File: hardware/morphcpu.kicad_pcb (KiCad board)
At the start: 4 copper layers, 70 x 70 mm, 84 parts, among them J1 TYPE-C-31-M-12, SW1 TS-1187A-B-A-B, U1 ICE40UP5K-SG48I, U2 FT231XS-R, U3 W25Q32JVSSIQ, U4 ME6211C33M5G-N, U5 ME6211C12M5G-N, U6 USBLC6-2SC6, X1 1532H4-16000JWPDTSNL

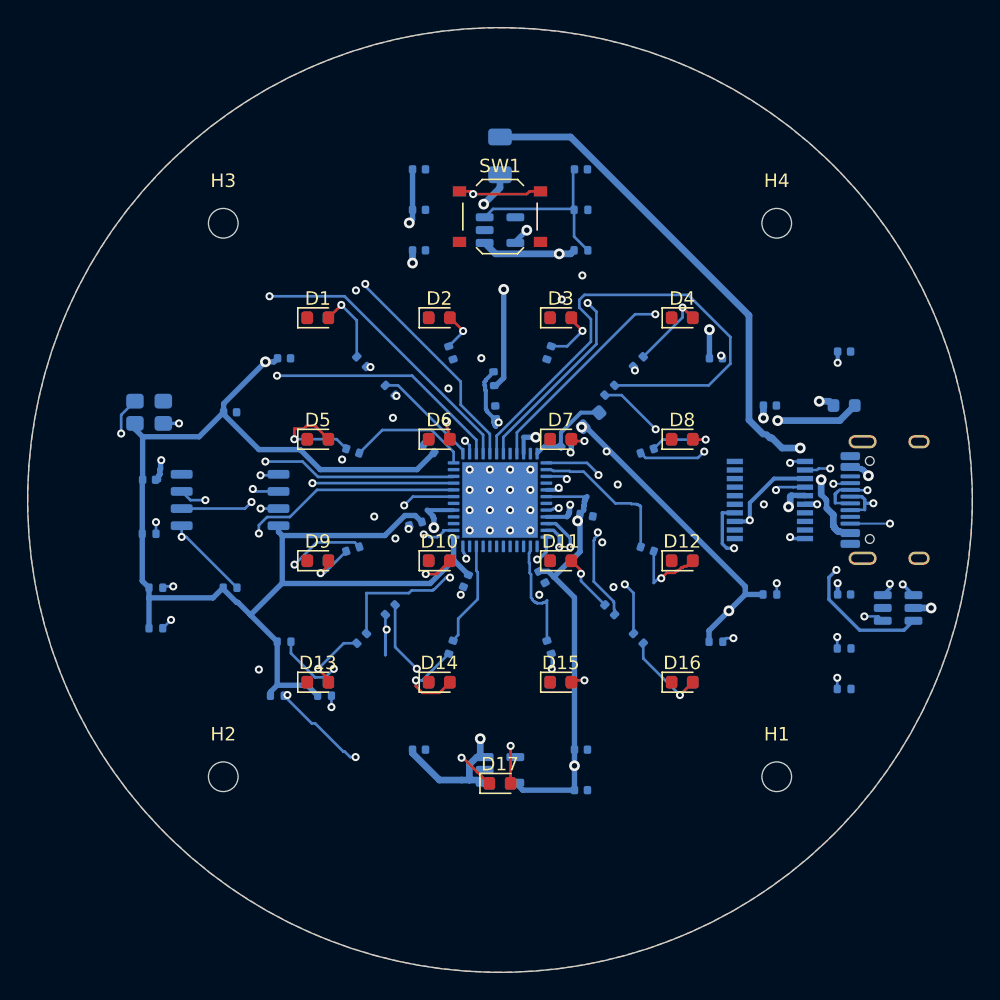
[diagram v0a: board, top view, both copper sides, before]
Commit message: silkscreen / board had none
only graphic on it was the edge cuts circle. front gets the name as eight
separate texts round r=29.7 rotated to the tangent cuz kicad has no curved
text, a frame circle at 32.9, IN and OUT arrows on the side lobes and eight
boxed direction arrows for what a cell can pick

back gets the name up top, url and iCE40UP5K SG48 and rev straight in the
bottom band. no frame circle that side, it crossed J1's outline at 182,95.3
and 182,104.7

mirrored arc text needs the run reversed and not just the glyphs, first pass
read UPCHPROM. first back pass also put the url's c and t into the H3 and H4
NPTH pads, 4 silk warnings, both gone now

DRC 0 violations, 2 unconnected, same two leds as before. no copper moved
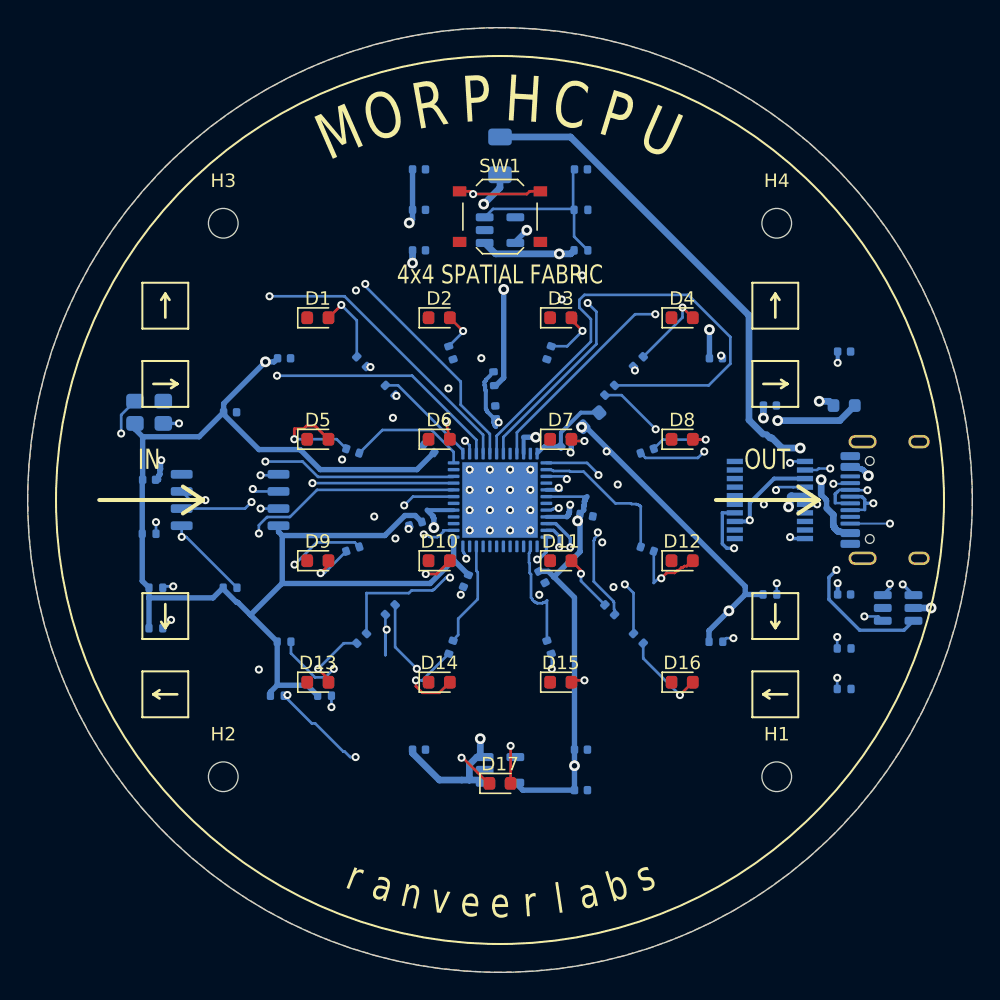
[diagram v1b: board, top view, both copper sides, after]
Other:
- board text added: "4x4 SPATIAL FABRIC"
- board text added: "C"
- board text added: "H"
- board text added: "IN"
- board text added: "M"
- board text added: "O"
- board text added: "OUT"
- board text added: "P"
- board text added: "R"
- board text added: "U"
- board text added: "a"
- board text added: "b"
- board text added: "e"
- board text added: "github.com/ranveerlabs/morphcpu"
- board text added: "iCE40UP5K SG48"
- board text added: "l"
- board text added: "n"
- board text added: "r"
- board text added: "rev A 2026"
- board text added: "s"
- board text added: "v"

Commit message: rev A off the back
sch_revision is empty and theres no earlier spin, so the board was carrying a
revision letter that nothing in the project backs. url and iCE40UP5K SG48 stay

DRC 0 violations, 2 unconnected, unchanged
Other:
- board text removed: "rev A 2026"
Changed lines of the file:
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@@
-		)
-	)
-	(gr_text "rev A  2026"
-		(at 150 131.199999 0)
-		(layer "B.SilkS")
-		(effects
-			(font
-				(size 1.3 1.014)
-				(thickness 0.22)
-			)
-			(justify mirror)
 		)
 	)

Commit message: decoupling caps onto their pins / stitching vias
the 6.5mm ring in gen_pcb.py placed the seven 100n by refdes order, so which
cap landed near which supply pin was arbitrary. measured as real copper path
not straight line, pin 22 was being decoupled by C12 under the FT231X at
49.31mm and pin 33 at 49.73mm. C4 and C5 were dead end spurs off the west
+3V3 trunk doing nothing for U1 at all

C3 -> pin 1 3.23 -> 1.16mm, C5 -> pin 22 49.31 -> 1.98mm, C21 -> pin 24
1.99 -> 1.13mm. deleted C5's 14.8mm dead end out to 132.14,96.27 and the
3.8mm stub it left dangling

every cap ground pad now has a via within 0.50mm with a 0.4mm tie so it
bypasses the thermal relief. C20 was 3.69mm off the nearest one and C5 3.03mm,
that was most of their loop

27 stitching vias at B.Cu island crossings under In2 traces. In2 references
B.Cu at 0.21mm and that pour is in 7 pieces, so a trace crossing a split had
the return current detouring to the nearest via. CRESET_B at 132.13,107.32 was
16.27mm and FLASH_HOLD at 126.84,107.68 was 15.11mm, both under 2mm now. two
crossings had no room, VBUS at 145.02,88.69 and +1V2 at 151.55,97.19

0 violations, 2 unrouted, same two LED nets as before
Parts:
- moved C5 8.47 mm to (153.1, 94.7), turned to 0 degrees
- moved C3 3.22 mm to (145.3, 103.7), turned to 180 degrees
- moved C21 0.83 mm to (154.1, 95.8), turned to 0 degrees
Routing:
- net +3V3: track 208.3 -> 192.3 mm
- net GND: track 4.70 -> 9.15 mm, vias 30 -> 64
- net VPP_2V5: track 6.44 -> 5.93 mm

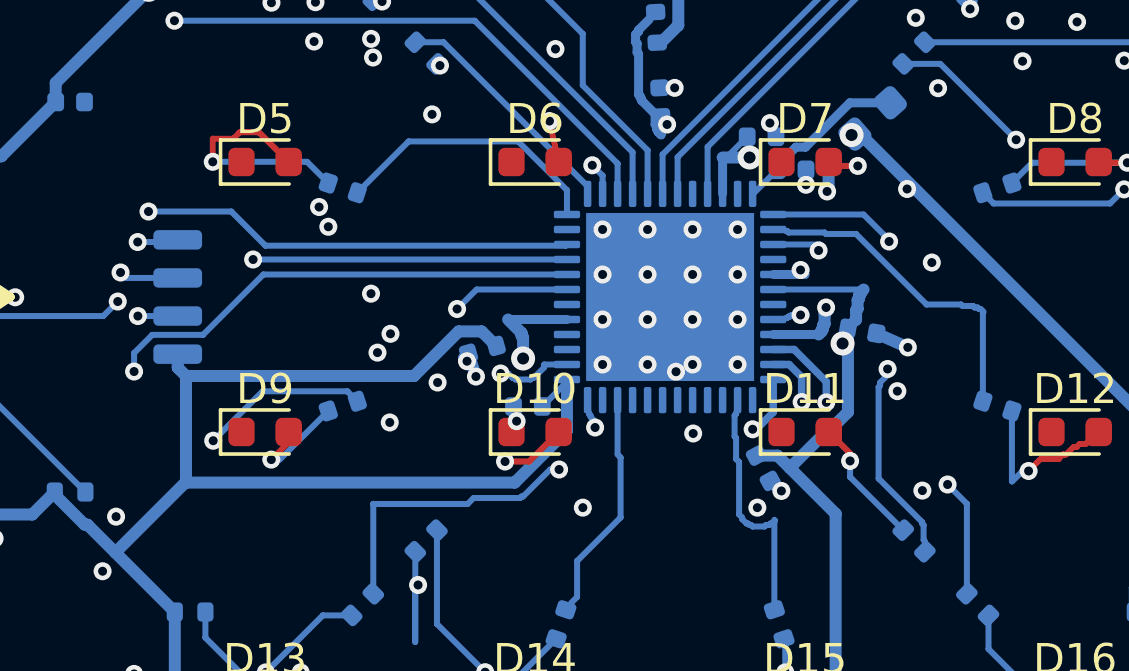
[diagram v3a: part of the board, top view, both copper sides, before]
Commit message: east face reshuffle / C4 across to pin 33
pins 29 30 and 33 all escape east and the lane at x 154-157 was full, so none
of them could have a cap next to them. moved the caps out to x=155.5375 instead
of hard against the pad row and most of the lane traffic stopped mattering

C1 -> pin 30, 156.401,101.129 -> 155.5375,99.90, path 3.24 -> 1.47mm
C4 -> pin 33, 143.743,101.760 -> 155.5375,101.25, path 49.73 -> 1.62mm
C2 -> pin 5, 153.109,105.708 -> 144.9625,100.75, path 13.77 -> 1.12mm

C4 crossing the board took its 11.2mm west dead end spur with it, and that spur
was what walled C2's ground pad onto a 1.58mm2 scrap of B.Cu pour with no room
for a via anywhere inside it. with the spur gone C2 has 251 placements with a
ground via, it had 0

LED11 LED15 and UART_TX_O did not need touching. checked each against the new
pads, LED11 clears C20 by 0.59mm, LED15's via at 154.350,100.600 sits 0.279mm
off C1 and 0.246mm off C4, UART clears C4 by 0.464mm. left as routed

three feeds rebuilt. +1V2 from the U5 trunk tip 7.11mm on In2 necked to 0.30
through the 0.72mm gap between LED15's via and C1's ground pad, the In1 tie to
pin 5 re-landed 5.24mm, +3V3 out of C4 6.22mm on In1 to the B.Cu diagonal

pin 29 still has no cap. with LED3 where it is C20 has 582 positions where it
fits with a clear courtyard and 0 with a routable stub. strip LED3 and C20
places at 1.76mm, but LED3's only via pocket is x 154.6-155.3 y 98.2-98.8 which
is exactly under C20's pad, and it cant go up either, a via between LED10 at
97.25 and LED3 at 98.25 needs 0.6mm clear of both which leaves nothing

one more stitching via, VBUS at 145.02,97.91, 4.97 -> 0.91mm. that crossing is
new, pulling C4's spur reshaped the pour there

six of seven supply pins under 2mm now. 0 violations, 2 unrouted
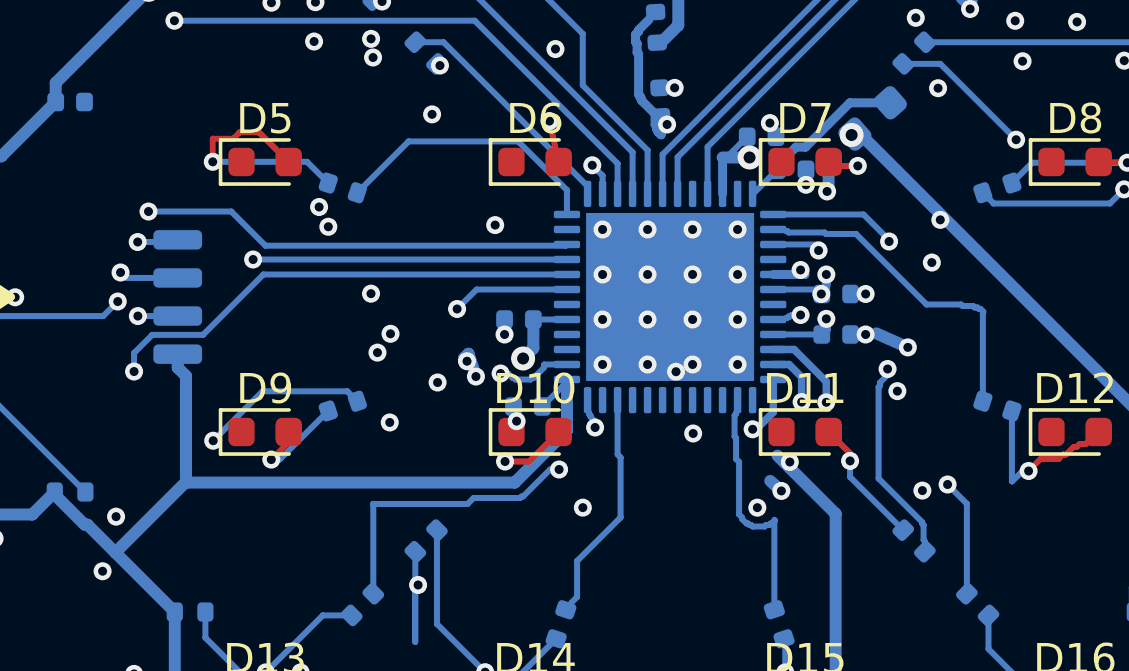
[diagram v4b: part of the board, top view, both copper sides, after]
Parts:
- moved C4 11.8 mm to (155.5, 101.2), turned to 0 degrees
- moved C2 9.54 mm to (145.0, 100.8), turned to 180 degrees
- moved C1 1.50 mm to (155.5, 99.9), turned to 0 degrees
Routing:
- net +3V3: track 192.3 -> 181.4 mm
- net +1V2: track 91.3 -> 94.0 mm, vias 4 -> 6
- net GND: track 9.15 -> 10.6 mm, vias 64 -> 68

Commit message: 2 LEDSS!!!1!!!1!
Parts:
- C1, C10, C11, C12, C13, C14, C15, C16, C17, C18, C19, C2, C20, C21, C3, C4, C5, C6, C7, C8, C9: footprint C_0402_1005Metric -> Capacitor_SMD:C_0402_1005Metric
- D1, D10, D11, D12, D13, D14, D15, D16, D17, D2, D3, D4, D5, D6, D7, D8, D9: footprint LED_0603_1608Metric -> LED_SMD:LED_0603_1608Metric
- F1: footprint Fuse_1206_3216Metric -> Fuse:Fuse_1206_3216Metric
- FB1, FB2: footprint L_0603_1608Metric -> Inductor_SMD:L_0603_1608Metric
- H1, H2, H3, H4: footprint MountingHole_2.2mm_M2 -> MountingHole:MountingHole_2.2mm_M2
- J1: footprint USB_C_Receptacle_HRO_TYPE-C-31-M-12 -> Connector_USB:USB_C_Receptacle_HRO_TYPE-C-31-M-12
- R1, R10, R11, R12, R13, R14, R15, R16, R17, R18, R19, R2, R20, R21, R22, R23, R24, R25, R27, R28, R29, R3, R30, R4, R5, R6, R7, R8, R9: footprint R_0402_1005Metric -> Resistor_SMD:R_0402_1005Metric
- R26: value 10k -> 1M; footprint R_0402_1005Metric -> Resistor_SMD:R_0402_1005Metric
- SW1: footprint SW_Push_1P1T_XKB_TS-1187A -> Button_Switch_SMD:SW_Push_1P1T_XKB_TS-1187A
- U1: footprint QFN-48-1EP_7x7mm_P0.5mm_EP5.6x5.6mm -> Package_DFN_QFN:QFN-48-1EP_7x7mm_P0.5mm_EP5.6x5.6mm
- U2: footprint SSOP-20_3.9x8.7mm_P0.635mm -> Package_SO:SSOP-20_3.9x8.7mm_P0.635mm
- U3: footprint SOIC-8_5.3x5.3mm_P1.27mm -> Package_SO:SOIC-8_5.3x5.3mm_P1.27mm
- U4: value ME6211C33M5G-N -> AP2112K-3.3TRG1; footprint SOT-23-5 -> Package_TO_SOT_SMD:SOT-23-5
- U5: footprint SOT-23-5 -> Package_TO_SOT_SMD:SOT-23-5
- U6: footprint SOT-23-6 -> Package_TO_SOT_SMD:SOT-23-6
- X1: footprint Oscillator_SMD_Abracon_ASE-4Pin_3.2x2.5mm -> Oscillator:Oscillator_SMD_Abracon_ASE-4Pin_3.2x2.5mm
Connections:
- U1 pad 23: LED2 -> unconnected-(U1A-IOT_37a-Pad23)
- U1 pad 3: LED1 -> unconnected-(U1C-IOB_9b-Pad3)
- U1 pad 42: unconnected-(U1A-IOT_51a-Pad42) -> LED2
- U1 pad 45: unconnected-(U1C-IOB_5b-Pad45) -> LED1
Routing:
- net LED2: track 0.00 -> 23.7 mm, vias 0 -> 3
- net LED1: track 0.00 -> 17.0 mm, vias 0 -> 2
- net LED9: track 29.9 -> 26.5 mm
- net LED4: track 9.18 -> 7.29 mm
- net GND: track 10.6 -> 9.35 mm
- net VBUS: track 119.3 -> 118.3 mm
- net +3V3: track 181.4 -> 180.5 mm
- net VBUS_IN: track 49.6 -> 50.2 mm
- net CDONE: track 38.5 -> 39.1 mm
- net VCCPLL_F: track 12.9 -> 12.4 mm

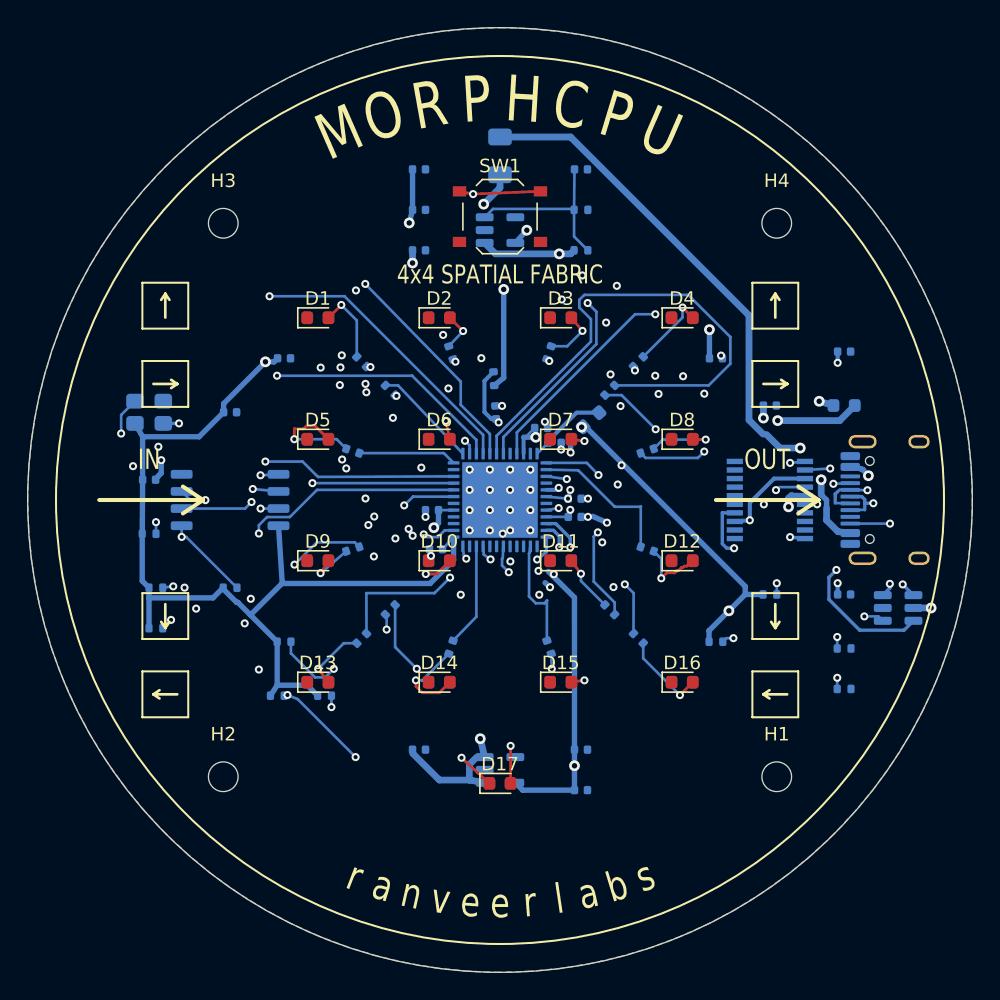
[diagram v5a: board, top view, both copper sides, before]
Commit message: kinda helvetica
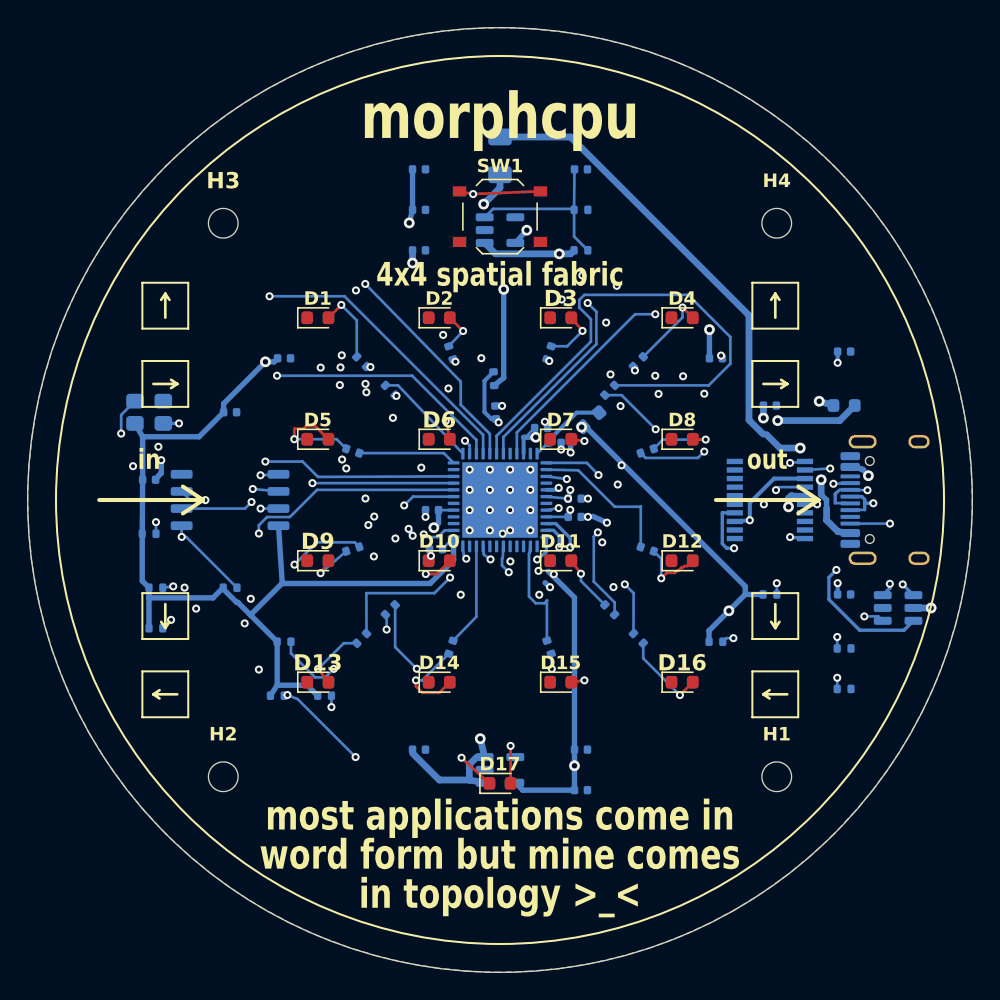
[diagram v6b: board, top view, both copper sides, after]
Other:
- board text added: "4x4 spatial fabric"
- board text added: "by ranveer gill"
- board text added: "ice40up5k sg48"
- board text added: "in"
- board text added: "in topology >_<"
- board text added: "morphcpu"
- board text added: "most applications come in"
- board text added: "out"
- board text added: "word form but mine comes"
- board text removed: "4x4 SPATIAL FABRIC"
- board text removed: "C"
- board text removed: "H"
- board text removed: "IN"
- board text removed: "M"
- board text removed: "O"
- board text removed: "OUT"
- board text removed: "P"
- board text removed: "R"
- board text removed: "U"
- board text removed: "a"
- board text removed: "b"
- board text removed: "e"
- board text removed: "iCE40UP5K SG48"
- board text removed: "l"
- board text removed: "n"
- board text removed: "r"
- board text removed: "s"
- board text removed: "v"

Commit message: cafe architecture -_-
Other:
- board text removed: "4x4 spatial fabric"
- board text removed: "github.com/ranveerlabs/morphcpu"
- board text removed: "ice40up5k sg48"
- board text removed: "in"
- board text removed: "out"
